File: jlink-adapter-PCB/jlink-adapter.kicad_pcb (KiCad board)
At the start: 2 copper layers, 15.5 x 27 mm, 13 parts, among them J1 Conn_02x10_Odd_Even, J2 Conn_02x05_Odd_Even, J3 Conn_02x05_Odd_Even, Q1 BSS123TA

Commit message: Add ECO comments from V1 fab and build.
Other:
- board text added: "Extend notch indicator outside of soldermask cutout"
- board text added: "Move R4 North to allow easier soldering"
- board text added: "Widen board by x.x mm To support connector"
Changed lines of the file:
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@@
       ))
   )
+  (gr_line (start 59.1 64.3) (end 59.2 93.65)
+    (stroke (width 0.15) (type default)) (layer "Eco1.User"))
+  (gr_line (start 65.4 50.05) (end 74.3 43.85)
+    (stroke (width 0.15) (type default)) (layer "Eco1.User"))
+  (gr_line (start 52.35 69.7) (end 43.55 63.35)
+    (stroke (width 0.15) (type default)) (layer "Eco1.User"))
   (gr_rect (start 50 50) (end 65.5 77)
     (stroke (width 0.1) (type default)) (fill none) (layer "Edge.Cuts"))
@@
     (effects (font (size 1.5 1.5) (thickness 0.3)) (justify left))
   )
+  (gr_text "Extend notch indicator outside\nof soldermask cutout" (at 19.8 63.65) (layer "Eco1.User")
+    (effects (font (size 1 1) (thickness 0.15)) (justify left bottom))
+  )
+  (gr_text "Widen board by x.x mm\nTo support connector" (at 75.2 44.05) (layer "Eco1.User")
+    (effects (font (size 1 1) (thickness 0.15)) (justify left bottom))
+  )
+  (gr_text "Move R4 North to allow easier soldering" (at 58.35 95.45) (layer "Eco1.User")
+    (effects (font (size 1 1) (thickness 0.15)) (justify left bottom))
+  )
   (gr_text "Back, Assembly" (at 229.5 90) (layer "B.Fab")
     (effects (font (size 1.5 1.5) (thickness 0.3)) (justify left))
@@
     (pts (xy 50 50) (xy 50 77))
     (height 2.25)
-    (gr_text "1.06299 in" (at 46.6 63.5 90) (layer "Dwgs.User")
+    (gr_text "27.0 mm" (at 46.6 63.5 90) (layer "Dwgs.User")
       (effects (font (size 1 1) (thickness 0.15)))
     )
-    (format (prefix "") (suffix "") (units 3) (units_format 1) (precision 5))
+    (format (prefix "") (suffix "") (units 3) (units_format 1) (precision 1))
     (style (thickness 0.15) (arrow_length 1.27) (text_position_mode 0) (extension_height 0.58642) (extension_offset 0.5) keep_text_aligned)
   )
@@
     (pts (xy 50 50) (xy 65.5 50))
     (height -1.8)
-    (gr_text "0.6 in" (at 57.75 47.05) (layer "Dwgs.User")
+    (gr_text "15.5 mm" (at 57.75 47.05) (layer "Dwgs.User")
       (effects (font (size 1 1) (thickness 0.15)))
     )

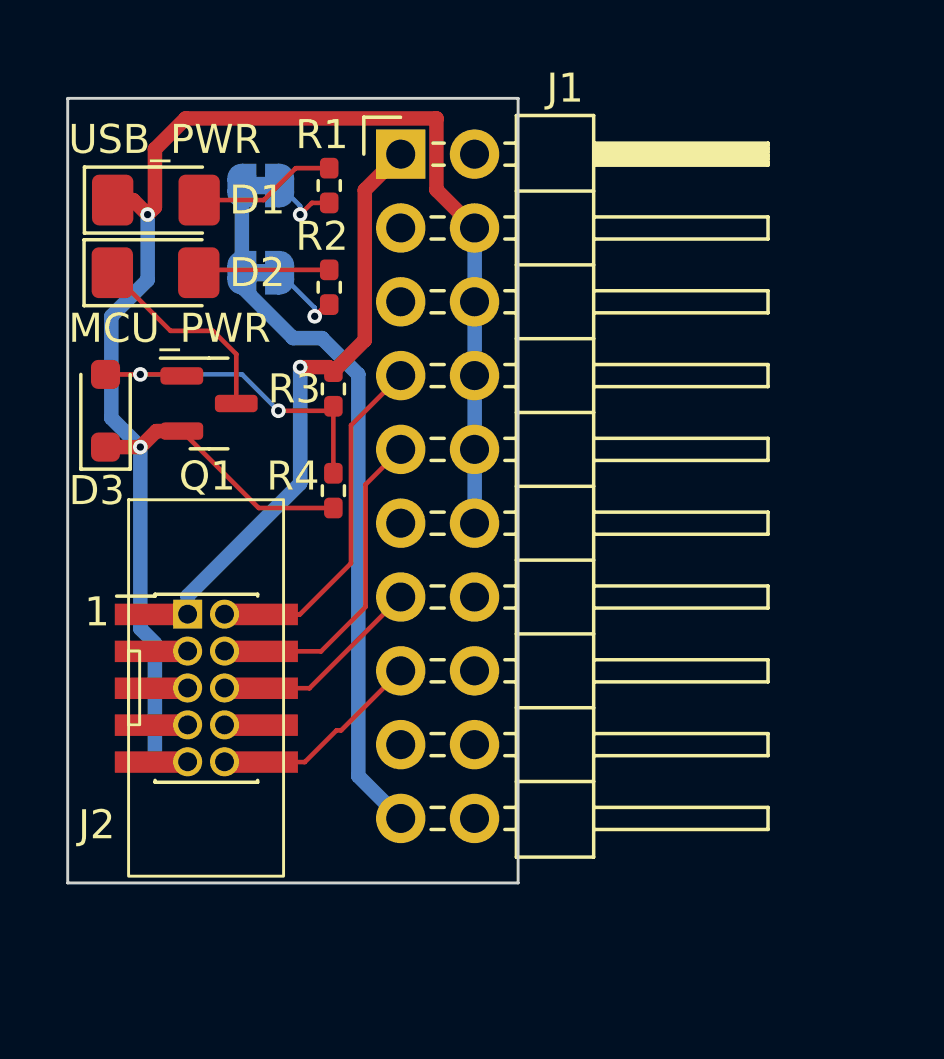
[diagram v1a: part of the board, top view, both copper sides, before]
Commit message: Re-layout PCB
* Changed to 4-layer board.
* Centered SWD connector
* Moved all non-user components to back-side
* Moved Jlink Connector in, instead of expanding board
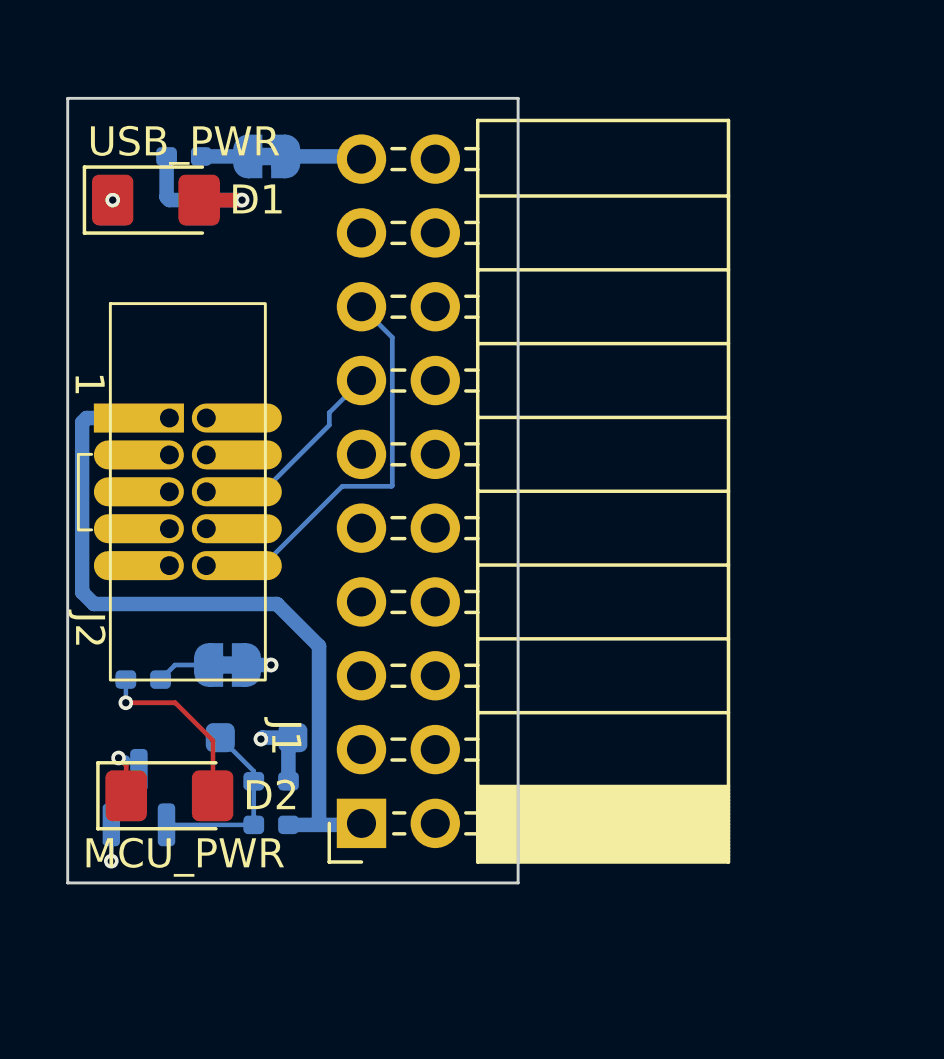
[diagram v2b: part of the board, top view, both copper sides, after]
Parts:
- removed J3: Conn_02x05_Odd_Even, Connector_PinHeader_1.27mm:PinHeader_2x05_P1.27mm_Vertical_SMD
- D3, Q1, R1, R2, R3, R4: moved to B.Cu
- J1: footprint Connector_PinHeader_2.54mm:PinHeader_2x10_P2.54mm_Horizontal -> Connector_PinSocket_2.54mm:PinSocket_2x10_P2.54mm_Horizontal
- moved J1 23.1 mm to (60.1, 75.0), turned to 180 degrees
- moved D2 18.0 mm to (53.5, 74.0)
- moved R3 15.2 mm to (57.0, 75.0), turned to 180 degrees
- moved R2 14.9 mm to (52.6, 70.0), turned to 180 degrees
- moved Q1 13.8 mm to (52.5, 74.1), turned to 90 degrees
- moved JP2 13.5 mm to (55.5, 69.5), turned to 0 degrees
- moved D3 12.4 mm to (56.5, 72.0), turned to 180 degrees
- moved R4 10.2 mm to (57.0, 73.5), turned to 0 degrees
- moved J2 6.78 mm to (53.5, 61.0)
- moved R1 5.10 mm to (54.0, 52.0), turned to 180 degrees
- moved JP1 1.02 mm to (56.9, 52.0), turned to 0 degrees
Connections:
- J2 pad 7: /NC_7 -> /KEY_(NC)
- J2 pad 8: /NC_8 -> /TDI
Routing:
- net GND: track 60.9 -> 3.93 mm, vias 2 -> 3
- net +5V: track 24.6 -> 3.50 mm, vias 0 -> 1
- net /RESET: track 6.04 -> 14.1 mm
- net /VTREF: track 19.8 -> 26.5 mm, vias 1 -> 0
- net Net-(D3-A2): track 12.2 -> 6.48 mm, vias 2 -> 0
- net Net-(D2-K): track 7.12 -> 2.28 mm, vias 0 -> 1
- net /SWCLK: track 10.1 -> 6.38 mm
- net /SWDIO: track 10.9 -> 12.9 mm
- net Net-(D2-A): track 4.53 -> 6.24 mm, vias 0 -> 1
- net /SWO: track 6.04 -> 7.18 mm
- net Net-(JP1-A): track 2.46 -> 1.60 mm, vias 1 -> 0
- net Net-(JP2-A): track 2.67 -> 1.86 mm, vias 1 -> 0
- net Net-(D1-A): track 4.93 -> 5.52 mm, vias 0 -> 1
- added copper zone on In2.Cu, net +5V
- added copper zone on In1.Cu, net GND
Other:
- copper layers 2 -> 4
- board text added: "SKEC V2"
- board text removed: "Extend notch indicator outside of soldermask cutout"
- board text removed: "MCU_PWR"
- board text removed: "Move R4 North to allow easier soldering"
- board text removed: "SKEC V1"
- board text removed: "USB_PWR"
- board text removed: "Widen board by x.x mm To support connector"

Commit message: Fix some DRC, tidy docs, and move a few traces.
Cleaned up and tidied the fabrication layer.

Also, decided to make the Front layer trace-free for aesthetics.  Did so
with via-in-pad for the LEDs.  This should be fine because this is being
hand soldered.
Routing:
- net Net-(D1-A): track 5.52 -> 2.56 mm
- net Net-(D2-K): track 2.28 -> 1.07 mm
- net Net-(D2-A): track 6.24 -> 5.26 mm
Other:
- board text added: "Back, Other Components"
- board text added: "Front, Connectors and LEDs"
- board text added: "In1 Copper, Ground Plane"
- board text added: "In2 Copper, 5V Plane"
- board text removed: "Back, [Description]"
- board text removed: "Front, [Description]"

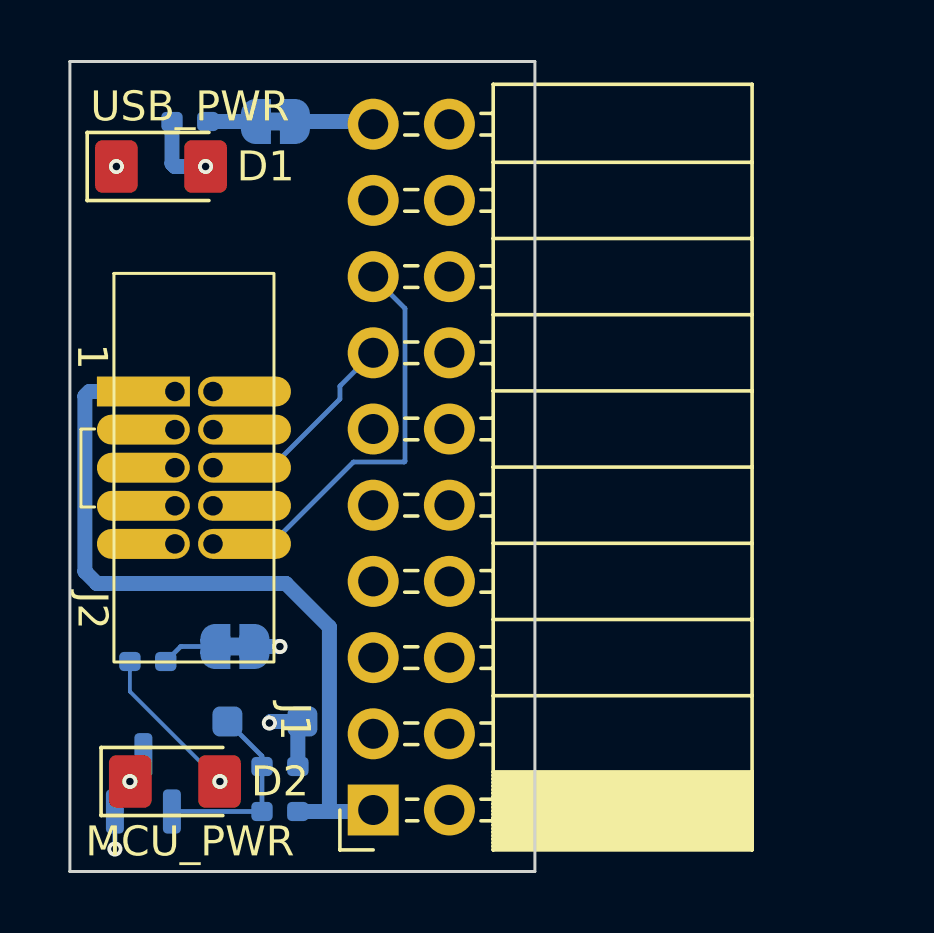
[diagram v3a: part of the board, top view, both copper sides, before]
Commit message: Finalize V2 of Jlink adapter
Cleaned up more DRC errors
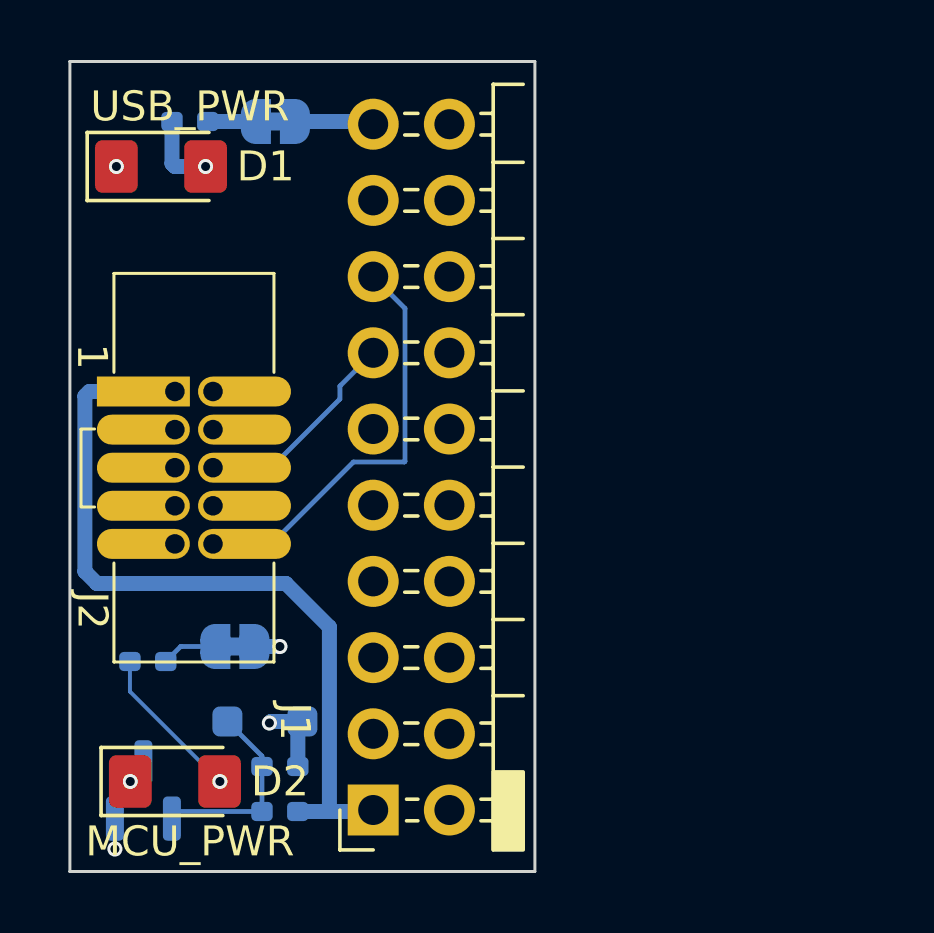
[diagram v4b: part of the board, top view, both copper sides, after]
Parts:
- J1: footprint Connector_PinSocket_2.54mm:PinSocket_2x10_P2.54mm_Horizontal -> JLink-adapter:PinSocket_2x10_P2.54mm_Horizontal_clipped_silkscreen
- moved Q1 0.24 mm to (52.5, 74.3)
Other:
- board text removed: "Back, Paste"
- board text removed: "Front, Paste"

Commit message: V1.0 of 2032 PCB
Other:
- board text added: "Reduce hole diameter a little"
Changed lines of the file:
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@@
     )
   )
+  (gr_line (start 59.85 75.2) (end 60.9 82.35)
+    (stroke (width 0.15) (type default)) (layer "Eco1.User"))
   (gr_rect (start 50 50) (end 65.5 77)
     (stroke (width 0.1) (type default)) (fill none) (layer "Edge.Cuts"))
@@
     (effects (font (size 1.5 1.5) (thickness 0.3)) (justify left))
   )
+  (gr_text "Reduce hole diameter a little" (at 59.8 83.75) (layer "Eco1.User")
+    (effects (font (size 1 1) (thickness 0.15)) (justify left bottom))
+  )
   (gr_text "Back, Assembly" (at 98 74) (layer "B.Fab")

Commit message: V3 of the Jlink board
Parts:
- added J3: Tag-Connect IDC, Connector_IDC:IDC-Header_2x03_P2.54mm_Vertical, F.Cu at (62.0, 61.0)
- added REF**: layer-label-4, SKEC_Footprints:layer-label-4-(F_B), F.Cu at (60.7, 52.8)
- moved J1 10.0 mm to (70.1, 75.0)
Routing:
- net /VTREF: track 26.5 -> 44.9 mm
- net /SWO: track 7.18 -> 23.2 mm
- net /SWDIO: track 12.9 -> 24.0 mm
- net /SWCLK: track 6.38 -> 16.5 mm
- net /RESET: track 14.1 -> 22.4 mm
- net +5V: track 3.50 -> 0.87 mm, vias 1 -> 2
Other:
- board size 15.5 x 27 mm -> 25.5 x 27 mm
- board text added: "SKEC V3"
- board text added: "SWD"
- board text added: "Tag Cnct"
- board text removed: "Reduce hole diameter a little"
- board text removed: "SKEC V2"
